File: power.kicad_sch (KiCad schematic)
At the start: 0 parts

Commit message: add power circuit
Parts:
- added C3, C4, C5: 10uF, symbol Device:C
- added D1: D, symbol Device:D
- added D2: LED, symbol Device:LED
- added R5: 100k, symbol Device:R
- added R6: 390, symbol Device:R
- added R7, R8: R, symbol Device:R
- added R9: 4.7k, symbol Device:R
- added U2: AP2112K-3.3TRG1, AP2112K-3.3TRG1:SOT95P285X140-5N, symbol AP2112K-3.3TRG1:AP2112K-3.3TRG1
- added U3: MCP73831T-2ACI/OT, SOT-23-5_MC_MCH, symbol MCP73831T-2ACI/OT:MCP73831T-2ACI_OT
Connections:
- new net: C4.1, U2.5 (VOUT)
- new net: C3.1, D1.1 (K), U2.1 (VIN), U2.3 (EN)
- new net: R8.2, U3.1 (STAT)
- new net: C5.2, U3.3 (VBAT)
- new net: D2.2 (A), U3.4 (VDD)
- new net: D1.2 (A), R5.1, R6.1
- new net: D2.1 (K), R8.1
- new net GND: C3.2, C4.2, R5.2, R7.1, R9.1, U2.2 (GND), U3.2 (VSS)
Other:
- note added: "3.3v"
- note added: "VUSB"
- note added: "Vbat"

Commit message: updatepower
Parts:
- U2: footprint AP2112K-3.3TRG1:SOT95P285X140-5N -> uSlime-libs:SOT95P285X140-5N; symbol AP2112K-3.3TRG1:AP2112K-3.3TRG1 -> uSlime:AP2112K-3.3TRG1
- U3: footprint SOT-23-5_MC_MCH -> uSlime-libs:SOT-23-5_MC_MCH; symbol MCP73831T-2ACI/OT:MCP73831T-2ACI_OT -> uSlime:MCP73831T-2ACI_OT
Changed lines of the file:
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@@
 	)
 	(symbol
-		(lib_id "MCP73831T-2ACI/OT:MCP73831T-2ACI_OT")
+		(lib_id "uSlime:MCP73831T-2ACI_OT")
 		(at 173.99 53.34 0)
 		(unit 1)
@@
 			)
 		)
-		(property "Footprint" "SOT-23-5_MC_MCH"
+		(property "Footprint" "uSlime-libs:SOT-23-5_MC_MCH"
 			(at 173.99 53.34 0)
 			(effects
@@
 	)
 	(symbol
-		(lib_id "AP2112K-3.3TRG1:AP2112K-3.3TRG1")
+		(lib_id "uSlime:AP2112K-3.3TRG1")
 		(at 81.28 111.76 0)
 		(unit 1)
@@
 			)
 		)
-		(property "Footprint" "AP2112K-3.3TRG1:SOT95P285X140-5N"
+		(property "Footprint" "uSlime-libs:SOT95P285X140-5N"
 			(at 81.28 111.76 0)
 			(effects

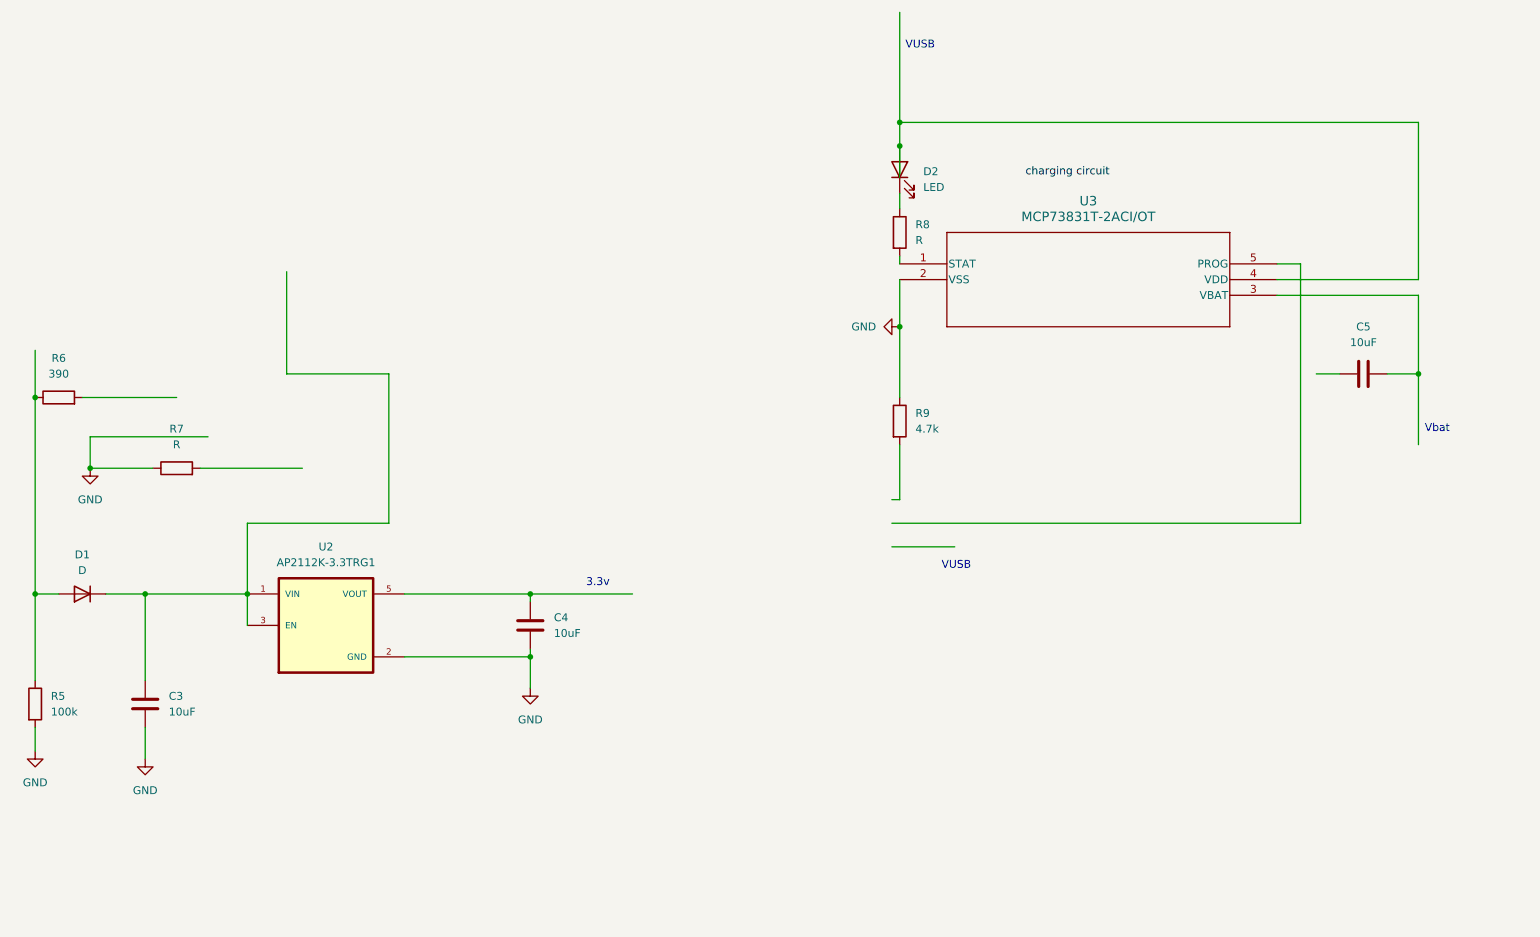
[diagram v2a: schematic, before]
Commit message: Update schematic and libraries
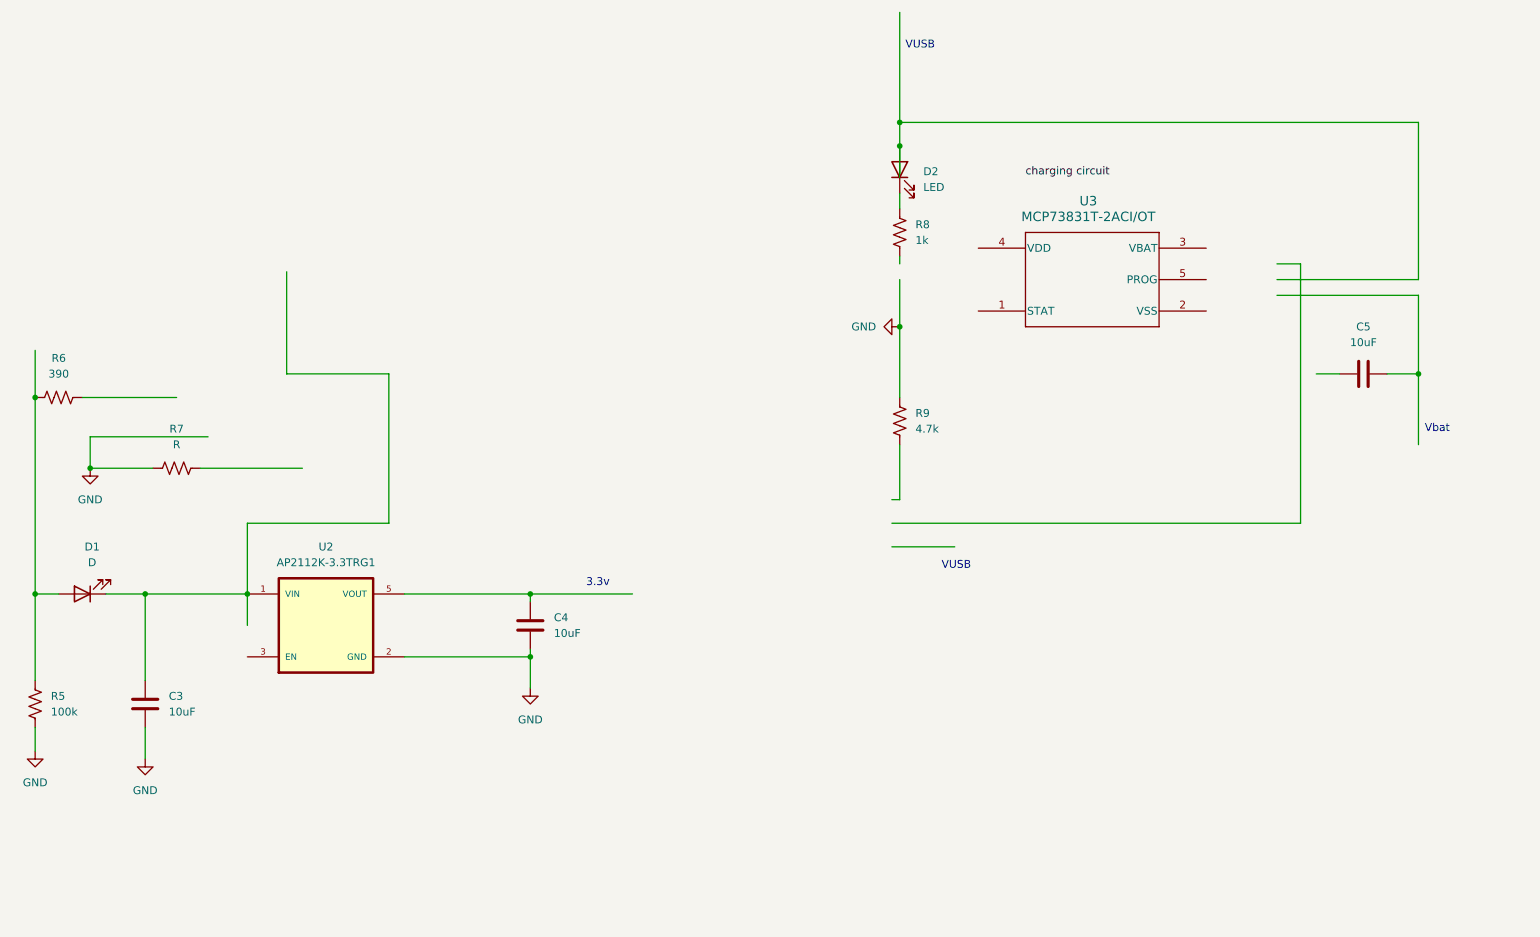
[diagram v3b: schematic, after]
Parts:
- C3, C4, C5: footprint (none) -> Capacitor_SMD:C_0603_1608Metric; symbol Device:C -> uSlime:C
- D1: footprint (none) -> LED_SMD:LED_0402_1005Metric; symbol Device:D -> uSlime:LED
- D2: footprint (none) -> LED_SMD:LED_0402_1005Metric; symbol Device:LED -> uSlime:LED
- R5, R6, R7, R9: footprint (none) -> Resistor_SMD:R_0603_1608Metric; symbol Device:R -> uSlime:R_US
- R8: value R -> 1k; footprint (none) -> Resistor_SMD:R_0603_1608Metric; symbol Device:R -> uSlime:R_US
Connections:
- net GND: no longer U3.2 (VSS)
- net at C3.1, D1.1 (K), U2.1 (VIN): no longer U2.3 (EN)
- net at U3.1 (STAT): no longer R8.2
- net at U3.3 (VBAT): no longer C5.2
- net at U3.4 (VDD): no longer D2.2 (A)
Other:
- moved on the sheet: U3
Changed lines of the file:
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@@
 	)
 	(symbol
-		(lib_id "Device:C")
+		(lib_id "uSlime:C")
 		(at 114.3 111.76 0)
 		(unit 1)
@@
 			)
 		)
-		(property "Footprint" ""
+		(property "Footprint" "Capacitor_SMD:C_0603_1608Metric"
 			(at 115.2652 115.57 0)
 			(effects
@@
 	)
 	(symbol
-		(lib_id "Device:C")
+		(lib_id "uSlime:C")
 		(at 52.07 124.46 0)
 		(unit 1)
@@
 			)
 		)
-		(property "Footprint" ""
+		(property "Footprint" "Capacitor_SMD:C_0603_1608Metric"
 			(at 53.0352 128.27 0)
 			(effects
@@
 	)
 	(symbol
-		(lib_id "Device:R")
+		(lib_id "uSlime:R_US")
 		(at 34.29 124.46 0)
 		(unit 1)
@@
 			)
 		)
-		(property "Footprint" ""
-			(at 32.512 124.46 90)
+		(property "Footprint" "Resistor_SMD:R_0603_1608Metric"
+			(at 35.306 124.714 90)
 			(effects
 				(font
@@
 			)
 		)
-		(property "Description" "Resistor"
+		(property "Description" "Resistor, US symbol"
 			(at 34.29 124.46 0)
 			(effects
@@
 	)
 	(symbol
-		(lib_id "Device:R")
+		(lib_id "uSlime:R_US")
 		(at 57.15 86.36 90)
 		(unit 1)
@@
 			)
 		)
-		(property "Footprint" ""
-			(at 57.15 88.138 90)
+		(property "Footprint" "Resistor_SMD:R_0603_1608Metric"
+			(at 57.404 85.344 90)
 			(effects
 				(font
@@
 			)
 		)
-		(property "Description" "Resistor"
+		(property "Description" "Resistor, US symbol"
 			(at 57.15 86.36 0)
 			(effects
@@
 	)
 	(symbol
-		(lib_id "Device:LED")
+		(lib_id "uSlime:LED")
 		(at 173.99 38.1 90)
 		(unit 1)
@@
 			)
 		)
-		(property "Footprint" ""
+		(property "Footprint" "LED_SMD:LED_0402_1005Metric"
 			(at 173.99 38.1 0)
 			(effects
@@
 	)
 	(symbol
-		(lib_id "Device:C")
+		(lib_id "uSlime:C")
 		(at 248.92 71.12 90)
 		(unit 1)
@@
 			)
 		)
-		(property "Footprint" ""
+		(property "Footprint" "Capacitor_SMD:C_0603_1608Metric"
 			(at 252.73 70.1548 0)
 			(effects
@@
 	)
 	(symbol
-		(lib_id "Device:R")
+		(lib_id "uSlime:R_US")
 		(at 173.99 78.74 0)
 		(unit 1)
@@
 			)
 		)
-		(property "Footprint" ""
-			(at 172.212 78.74 90)
+		(property "Footprint" "Resistor_SMD:R_0603_1608Metric"
+			(at 175.006 78.994 90)
 			(effects
 				(font
@@
 			)
 		)
-		(property "Description" "Resistor"
+		(property "Description" "Resistor, US symbol"
 			(at 173.99 78.74 0)
 			(effects
@@
 	)
 	(symbol
-		(lib_id "Device:D")
+		(lib_id "uSlime:LED")
 		(at 41.91 106.68 180)
 		(unit 1)
@@
 		(fields_autoplaced yes)
 		(property "Reference" "D1"
-			(at 41.91 100.33 0)
+			(at 43.4975 99.06 0)
 			(effects
 				(font
@@
 		)
 		(property "Value" "D"
-			(at 41.91 102.87 0)
-			(effects
-				(font
-					(size 1.27 1.27)
-				)
-			)
-		)
-		(property "Footprint" ""
+			(at 43.4975 101.6 0)
+			(effects
+				(font
+					(size 1.27 1.27)
+				)
+			)
+		)
+		(property "Footprint" "LED_SMD:LED_0402_1005Metric"
 			(at 41.91 106.68 0)
 			(effects
@@
 			)
 		)
-		(property "Description" "Diode"
+		(property "Description" "Light emitting diode"
 			(at 41.91 106.68 0)
 			(effects
@@
 	)
 	(symbol
-		(lib_id "Device:R")
+		(lib_id "uSlime:R_US")
 		(at 38.1 74.93 90)
 		(unit 1)
@@
 			)
 		)
-		(property "Footprint" ""
-			(at 38.1 76.708 90)
+		(property "Footprint" "Resistor_SMD:R_0603_1608Metric"
+			(at 38.354 73.914 90)
 			(effects
 				(font
@@
 			)
 		)
-		(property "Description" "Resistor"
+		(property "Description" "Resistor, US symbol"
 			(at 38.1 74.93 0)
 			(effects
@@
 	)
 	(symbol
-		(lib_id "Device:R")
+		(lib_id "uSlime:R_US")
 		(at 173.99 48.26 0)
 		(unit 1)
@@
 			)
 		)
-		(property "Value" "R"
+		(property "Value" "1k"
 			(at 176.53 49.5299 0)
 			(effects
@@
 			)
 		)
-		(property "Footprint" ""
-			(at 172.212 48.26 90)
+		(property "Footprint" "Resistor_SMD:R_0603_1608Metric"
+			(at 175.006 48.514 90)
 			(effects
 				(font
@@
 			)
 		)
-		(property "Description" "Resistor"
+		(property "Description" "Resistor, US symbol"
 			(at 173.99 48.26 0)
 			(effects

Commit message: Update power.kicad_sch
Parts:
- added J2: USB_B_Micro, symbol Connector:USB_B_Micro
- C3, C4, C5: footprint Capacitor_SMD:C_0603_1608Metric -> (none); symbol uSlime:C -> Device:C
- D1: footprint LED_SMD:LED_0402_1005Metric -> (none); symbol uSlime:LED -> Device:D
- D2: footprint LED_SMD:LED_0402_1005Metric -> (none); symbol uSlime:LED -> Device:LED
- R5, R6, R7, R9: footprint Resistor_SMD:R_0603_1608Metric -> (none); symbol uSlime:R_US -> Device:R
- R8: value 1k -> R; footprint Resistor_SMD:R_0603_1608Metric -> (none); symbol uSlime:R_US -> Device:R
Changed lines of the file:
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@@
 	)
 	(symbol
-		(lib_id "uSlime:C")
+		(lib_id "Device:C")
 		(at 114.3 111.76 0)
 		(unit 1)
@@
 			)
 		)
-		(property "Footprint" "Capacitor_SMD:C_0603_1608Metric"
+		(property "Footprint" ""
 			(at 115.2652 115.57 0)
 			(effects
@@
 	)
 	(symbol
-		(lib_id "uSlime:C")
+		(lib_id "Device:C")
 		(at 52.07 124.46 0)
 		(unit 1)
@@
 			)
 		)
-		(property "Footprint" "Capacitor_SMD:C_0603_1608Metric"
+		(property "Footprint" ""
 			(at 53.0352 128.27 0)
 			(effects
@@
 	)
 	(symbol
-		(lib_id "uSlime:R_US")
+		(lib_id "Device:R")
 		(at 34.29 124.46 0)
 		(unit 1)
@@
 			)
 		)
-		(property "Footprint" "Resistor_SMD:R_0603_1608Metric"
-			(at 35.306 124.714 90)
+		(property "Footprint" ""
+			(at 32.512 124.46 90)
 			(effects
 				(font
@@
 			)
 		)
-		(property "Description" "Resistor, US symbol"
+		(property "Description" "Resistor"
 			(at 34.29 124.46 0)
 			(effects
@@
 	)
 	(symbol
-		(lib_id "uSlime:R_US")
+		(lib_id "Device:R")
 		(at 57.15 86.36 90)
 		(unit 1)
@@
 			)
 		)
-		(property "Footprint" "Resistor_SMD:R_0603_1608Metric"
-			(at 57.404 85.344 90)
+		(property "Footprint" ""
+			(at 57.15 88.138 90)
 			(effects
 				(font
@@
 			)
 		)
-		(property "Description" "Resistor, US symbol"
+		(property "Description" "Resistor"
 			(at 57.15 86.36 0)
 			(effects
@@
 	)
 	(symbol
-		(lib_id "uSlime:LED")
+		(lib_id "Device:LED")
 		(at 173.99 38.1 90)
 		(unit 1)
@@
 			)
 		)
-		(property "Footprint" "LED_SMD:LED_0402_1005Metric"
+		(property "Footprint" ""
 			(at 173.99 38.1 0)
 			(effects
@@
 	)
 	(symbol
-		(lib_id "uSlime:C")
+		(lib_id "Device:C")
 		(at 248.92 71.12 90)
 		(unit 1)
@@
 			)
 		)
-		(property "Footprint" "Capacitor_SMD:C_0603_1608Metric"
+		(property "Footprint" ""
 			(at 252.73 70.1548 0)
 			(effects
@@
 	)
 	(symbol
-		(lib_id "uSlime:R_US")
+		(lib_id "Device:R")
 		(at 173.99 78.74 0)
 		(unit 1)
@@
 			)
 		)
-		(property "Footprint" "Resistor_SMD:R_0603_1608Metric"
-			(at 175.006 78.994 90)
+		(property "Footprint" ""
+			(at 172.212 78.74 90)
 			(effects
 				(font
@@
 			)
 		)
-		(property "Description" "Resistor, US symbol"
+		(property "Description" "Resistor"
 			(at 173.99 78.74 0)
 			(effects
@@
 	)
 	(symbol
-		(lib_id "uSlime:LED")
+		(lib_id "Device:D")
 		(at 41.91 106.68 180)
 		(unit 1)
@@
 		(fields_autoplaced yes)
 		(property "Reference" "D1"
-			(at 43.4975 99.06 0)
+			(at 41.91 100.33 0)
 			(effects
 				(font
@@
 		)
 		(property "Value" "D"
-			(at 43.4975 101.6 0)
-			(effects
-				(font
-					(size 1.27 1.27)
-				)
-			)
-		)
-		(property "Footprint" "LED_SMD:LED_0402_1005Metric"
+			(at 41.91 102.87 0)
+			(effects
+				(font
+					(size 1.27 1.27)
+				)
+			)
+		)
+		(property "Footprint" ""
 			(at 41.91 106.68 0)
 			(effects
@@
 			)
 		)
-		(property "Description" "Light emitting diode"
+		(property "Description" "Diode"
 			(at 41.91 106.68 0)
 			(effects
@@
 	)
 	(symbol
-		(lib_id "uSlime:R_US")
+		(lib_id "Device:R")
 		(at 38.1 74.93 90)
 		(unit 1)
@@
 			)
 		)
-		(property "Footprint" "Resistor_SMD:R_0603_1608Metric"
-			(at 38.354 73.914 90)
+		(property "Footprint" ""
+			(at 38.1 76.708 90)
 			(effects
 				(font
@@
 			)
 		)
-		(property "Description" "Resistor, US symbol"
+		(property "Description" "Resistor"
 			(at 38.1 74.93 0)
 			(effects
@@
 	)
 	(symbol
-		(lib_id "uSlime:R_US")
+		(lib_id "Connector:USB_B_Micro")
+		(at 207.01 127 0)
+		(unit 1)
+		(exclude_from_sim no)
+		(in_bom yes)
+		(on_board yes)
+		(dnp no)
+		(fields_autoplaced yes)
+		(property "Reference" "J2"
+			(at 207.01 114.3 0)
+			(effects
+				(font
+					(size 1.27 1.27)
+				)
+			)
+		)
+		(property "Value" "USB_B_Micro"
+			(at 207.01 116.84 0)
+			(effects
+				(font
+					(size 1.27 1.27)
+				)
+			)
+		)
+		(property "Footprint" ""
+			(at 210.82 128.27 0)
+			(effects
+				(font
+					(size 1.27 1.27)
+				)
+				(hide yes)
+			)
+		)
+		(property "Datasheet" "~"
+			(at 210.82 128.27 0)
+			(effects
+				(font
+					(size 1.27 1.27)
+				)
+				(hide yes)
+			)
+		)
+		(property "Description" "USB Micro Type B connector"
+			(at 207.01 127 0)
+			(effects
+				(font
+					(size 1.27 1.27)
+				)
+				(hide yes)
+			)
+		)
+		(pin "1"
+		)
+		(pin "2"
+		)
+		(pin "3"
+		)
+		(pin "4"
+		)
+		(pin "5"
+		)
+		(pin "6"
+		)
+		(instances
+			(project "uSlime"
+				(path "/f32c1c49-f803-4e7c-a530-6db148a7ba36/9141278c-15a6-43aa-8c9d-f1bdf7efadba"
+					(reference "J2")
+					(unit 1)
+				)
+			)
+		)
+	)
+	(symbol
+		(lib_id "Device:R")
 		(at 173.99 48.26 0)
 		(unit 1)
@@
 			)
 		)
-		(property "Value" "1k"
+		(property "Value" "R"
 			(at 176.53 49.5299 0)
 			(effects
@@
 			)
 		)
-		(property "Footprint" "Resistor_SMD:R_0603_1608Metric"
-			(at 175.006 48.514 90)
+		(property "Footprint" ""
+			(at 172.212 48.26 90)
 			(effects
 				(font
@@
 			)
 		)
-		(property "Description" "Resistor, US symbol"
+		(property "Description" "Resistor"
 			(at 173.99 48.26 0)
 			(effects
